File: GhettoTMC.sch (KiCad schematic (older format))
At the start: 48 parts

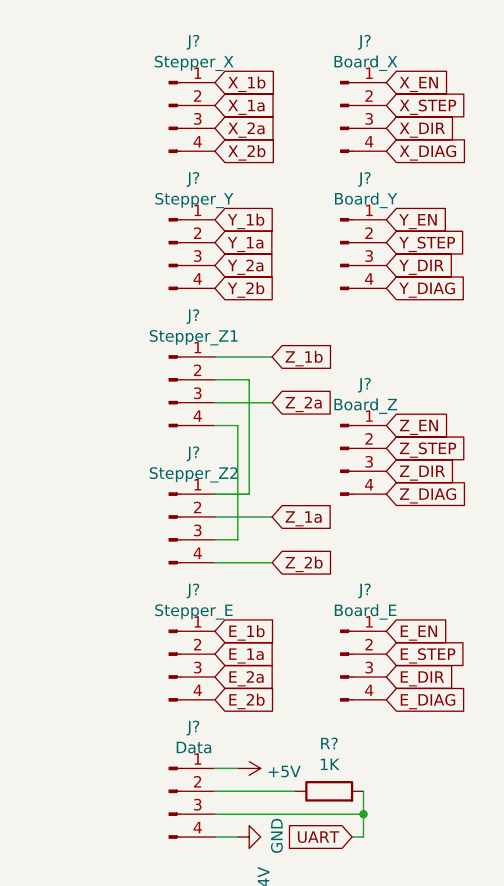
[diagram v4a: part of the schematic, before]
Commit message: Switch to 5p Board connectors
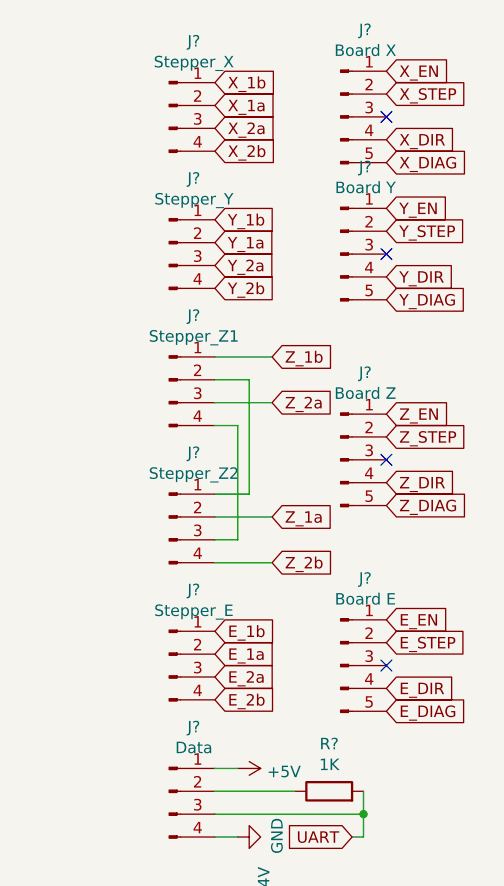
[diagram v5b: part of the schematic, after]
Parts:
- removed J?: Board_Y, GhettoTMC:MOLEX_70553-0038, symbol Connector:Conn_01x04_Male
- removed J?: Board_X, GhettoTMC:MOLEX_70553-0038, symbol Connector:Conn_01x04_Male
- removed J?: Board_Z, GhettoTMC:MOLEX_70553-0038, symbol Connector:Conn_01x04_Male
- removed J?: Board_E, GhettoTMC:MOLEX_70553-0038, symbol Connector:Conn_01x04_Male
- added J?: Board X, GhettoTMC:MOLEX_70553-0039, symbol Connector:Conn_01x05_Male
- added J?: Board Y, GhettoTMC:MOLEX_70553-0039, symbol Connector:Conn_01x05_Male
- added J?: Board Z, GhettoTMC:MOLEX_70553-0039, symbol Connector:Conn_01x05_Male
- added J?: Board E, GhettoTMC:MOLEX_70553-0039, symbol Connector:Conn_01x05_Male
- J?: footprint (none) -> Connectors_Phoenix:PhoenixContact_MC-G_02x5.08mm_Angled
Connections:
- net E_DIAG: now also J?.5 (Pin_5)
- net E_DIR: now also J?.4 (Pin_4)
- net E_EN: now also J?.1 (Pin_1)
- net E_STEP: now also J?.2 (Pin_2)
- net X_DIAG: now also J?.5 (Pin_5)
- net X_DIR: now also J?.4 (Pin_4)
- net X_EN: now also J?.1 (Pin_1)
- net X_STEP: now also J?.2 (Pin_2)
- net Y_DIAG: now also J?.5 (Pin_5)
- net Y_DIR: now also J?.4 (Pin_4)
- net Y_EN: now also J?.1 (Pin_1)
- net Y_STEP: now also J?.2 (Pin_2)
- net Z_DIAG: now also J?.5 (Pin_5)
- net Z_DIR: now also J?.4 (Pin_4)
- net Z_EN: now also J?.1 (Pin_1)
- net Z_STEP: now also J?.2 (Pin_2)
- no-connect marks 4 -> 8
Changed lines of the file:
@@
 	10000 4350 10000 4250
 Connection ~ 10000 4250
-$Comp
-L Connector:Conn_01x04_Male J?
-U 1 1 5EAC38CC
-P 9900 1750
-F 0 "J?" H 10008 2031 50  0000 C CNN
-F 1 "Board_Y" H 10008 1940 50  0000 C CNN
-F 2 "GhettoTMC:MOLEX_70553-0038" H 9900 1750 50  0001 C CNN
-F 3 "~" H 9900 1750 50  0001 C CNN
-	1    9900 1750
-	1    0    0    -1
-$EndComp
-$Comp
-L Connector:Conn_01x04_Male J?
-U 1 1 5EAC4D8C
-P 9900 1150
-F 0 "J?" H 10008 1431 50  0000 C CNN
-F 1 "Board_X" H 10008 1340 50  0000 C CNN
-F 2 "GhettoTMC:MOLEX_70553-0038" H 9900 1150 50  0001 C CNN
-F 3 "~" H 9900 1150 50  0001 C CNN
-	1    9900 1150
-	1    0    0    -1
-$EndComp
-$Comp
-L Connector:Conn_01x04_Male J?
-U 1 1 5EAC51EC
-P 9900 2650
-F 0 "J?" H 10008 2931 50  0000 C CNN
-F 1 "Board_Z" H 10008 2840 50  0000 C CNN
-F 2 "GhettoTMC:MOLEX_70553-0038" H 9900 2650 50  0001 C CNN
-F 3 "~" H 9900 2650 50  0001 C CNN
-	1    9900 2650
-	1    0    0    -1
-$EndComp
-$Comp
-L Connector:Conn_01x04_Male J?
-U 1 1 5EAC5E5C
-P 9900 3550
-F 0 "J?" H 10008 3831 50  0000 C CNN
-F 1 "Board_E" H 10008 3740 50  0000 C CNN
-F 2 "GhettoTMC:MOLEX_70553-0038" H 9900 3550 50  0001 C CNN
-F 3 "~" H 9900 3550 50  0001 C CNN
-	1    9900 3550
-	1    0    0    -1
-$EndComp
-Text GLabel 10100 1950 2    50   Input ~ 0
+Text GLabel 10100 2000 2    50   Input ~ 0
 Y_DIAG
-Text GLabel 10100 1850 2    50   Input ~ 0
+Text GLabel 10100 1900 2    50   Input ~ 0
 Y_DIR
-Text GLabel 10100 1650 2    50   Input ~ 0
+Text GLabel 10100 1600 2    50   Input ~ 0
 Y_EN
-Text GLabel 10100 1750 2    50   Input ~ 0
+Text GLabel 10100 1700 2    50   Input ~ 0
 Y_STEP
-Text GLabel 10100 1350 2    50   Input ~ 0
+Text GLabel 10100 1400 2    50   Input ~ 0
 X_DIAG
-Text GLabel 10100 1250 2    50   Input ~ 0
+Text GLabel 10100 1300 2    50   Input ~ 0
 X_DIR
-Text GLabel 10100 1050 2    50   Input ~ 0
+Text GLabel 10100 1000 2    50   Input ~ 0
 X_EN
-Text GLabel 10100 1150 2    50   Input ~ 0
+Text GLabel 10100 1100 2    50   Input ~ 0
 X_STEP
-Text GLabel 10100 2850 2    50   Input ~ 0
+Text GLabel 10100 2900 2    50   Input ~ 0
 Z_DIAG
-Text GLabel 10100 2750 2    50   Input ~ 0
+Text GLabel 10100 2800 2    50   Input ~ 0
 Z_DIR
-Text GLabel 10100 2550 2    50   Input ~ 0
+Text GLabel 10100 2500 2    50   Input ~ 0
 Z_EN
-Text GLabel 10100 2650 2    50   Input ~ 0
+Text GLabel 10100 2600 2    50   Input ~ 0
 Z_STEP
-Text GLabel 10100 3750 2    50   Input ~ 0
+Text GLabel 10100 3800 2    50   Input ~ 0
 E_DIAG
-Text GLabel 10100 3650 2    50   Input ~ 0
+Text GLabel 10100 3700 2    50   Input ~ 0
 E_DIR
-Text GLabel 10100 3450 2    50   Input ~ 0
+Text GLabel 10100 3400 2    50   Input ~ 0
 E_EN
-Text GLabel 10100 3550 2    50   Input ~ 0
+Text GLabel 10100 3500 2    50   Input ~ 0
 E_STEP
 $Comp
@@
 F 0 "J?" H 9258 4981 50  0000 C CNN
 F 1 "POWER IN" H 9258 4890 50  0000 C CNN
-F 2 "" H 9150 4800 50  0001 C CNN
+F 2 "Connectors_Phoenix:PhoenixContact_MC-G_02x5.08mm_Angled" H 9150 4800 50  0001 C CNN
 F 3 "~" H 9150 4800 50  0001 C CNN
 	1    9150 4800
@@
 	1    0    0    -1
 $EndComp
+NoConn ~ 10100 1200
+$Comp
+L Connector:Conn_01x05_Male J?
+U 1 1 5EB3A24B
+P 9900 1800
+F 0 "J?" H 10008 2181 50  0000 C CNN
+F 1 "Board Y" H 10008 2090 50  0000 C CNN
+F 2 "GhettoTMC:MOLEX_70553-0039" H 9900 1800 50  0001 C CNN
+F 3 "~" H 9900 1800 50  0001 C CNN
+	1    9900 1800
+	1    0    0    -1
+$EndComp
+NoConn ~ 10100 1800
+$Comp
+L Connector:Conn_01x05_Male J?
+U 1 1 5EB41CC3
+P 9900 2700
+F 0 "J?" H 10008 3081 50  0000 C CNN
+F 1 "Board Z" H 10008 2990 50  0000 C CNN
+F 2 "GhettoTMC:MOLEX_70553-0039" H 9900 2700 50  0001 C CNN
+F 3 "~" H 9900 2700 50  0001 C CNN
+	1    9900 2700
+	1    0    0    -1
+$EndComp
+NoConn ~ 10100 2700
+$Comp
+L Connector:Conn_01x05_Male J?
+U 1 1 5EB49933
+P 9900 3600
+F 0 "J?" H 10008 3981 50  0000 C CNN
+F 1 "Board E" H 10008 3890 50  0000 C CNN
+F 2 "GhettoTMC:MOLEX_70553-0039" H 9900 3600 50  0001 C CNN
+F 3 "~" H 9900 3600 50  0001 C CNN
+	1    9900 3600
+	1    0    0    -1
+$EndComp
+NoConn ~ 10100 3600
+$Comp
+L Connector:Conn_01x05_Male J?
+U 1 1 5EB1718C
+P 9900 1200
+F 0 "J?" H 10008 1581 50  0000 C CNN
+F 1 "Board X" H 10008 1490 50  0000 C CNN
+F 2 "GhettoTMC:MOLEX_70553-0039" H 9900 1200 50  0001 C CNN
+F 3 "~" H 9900 1200 50  0001 C CNN
+	1    9900 1200
+	1    0    0    -1
+$EndComp

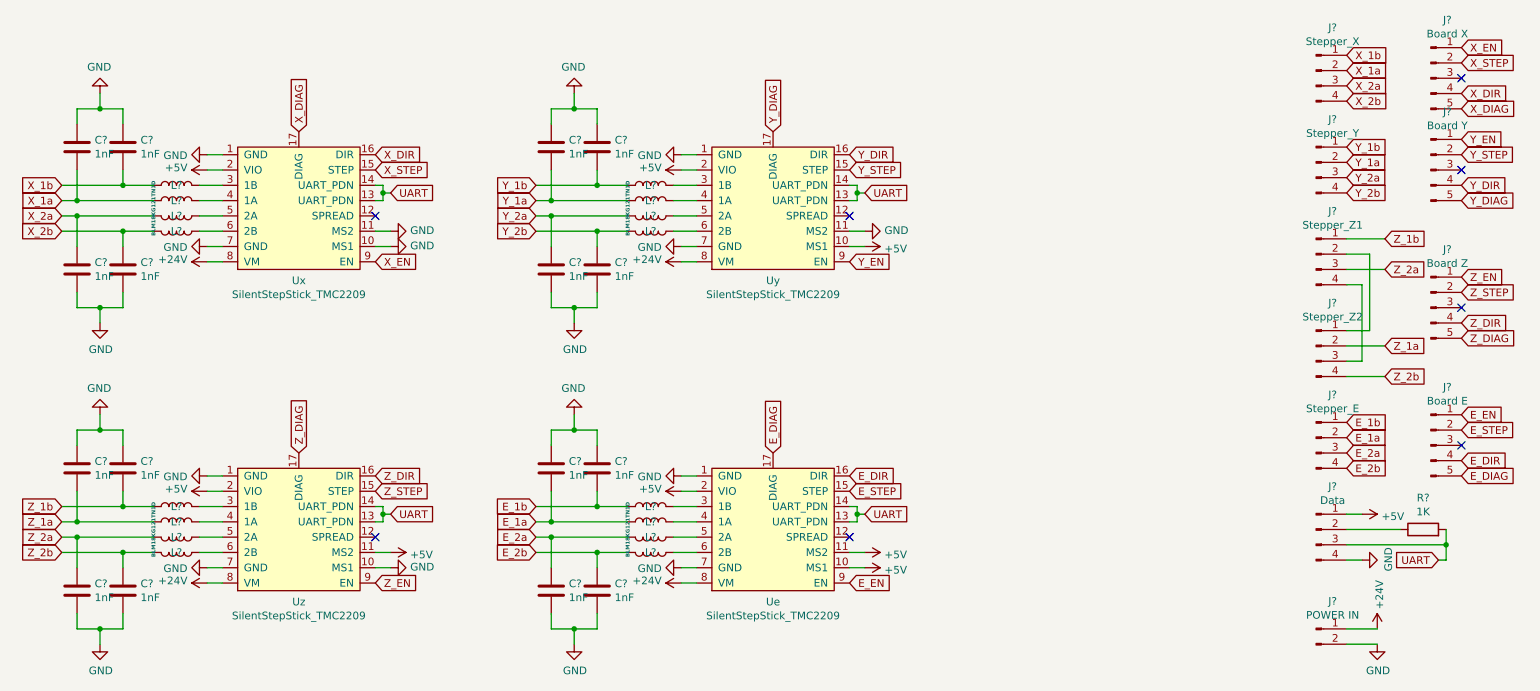
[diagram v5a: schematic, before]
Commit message: Assign footprints
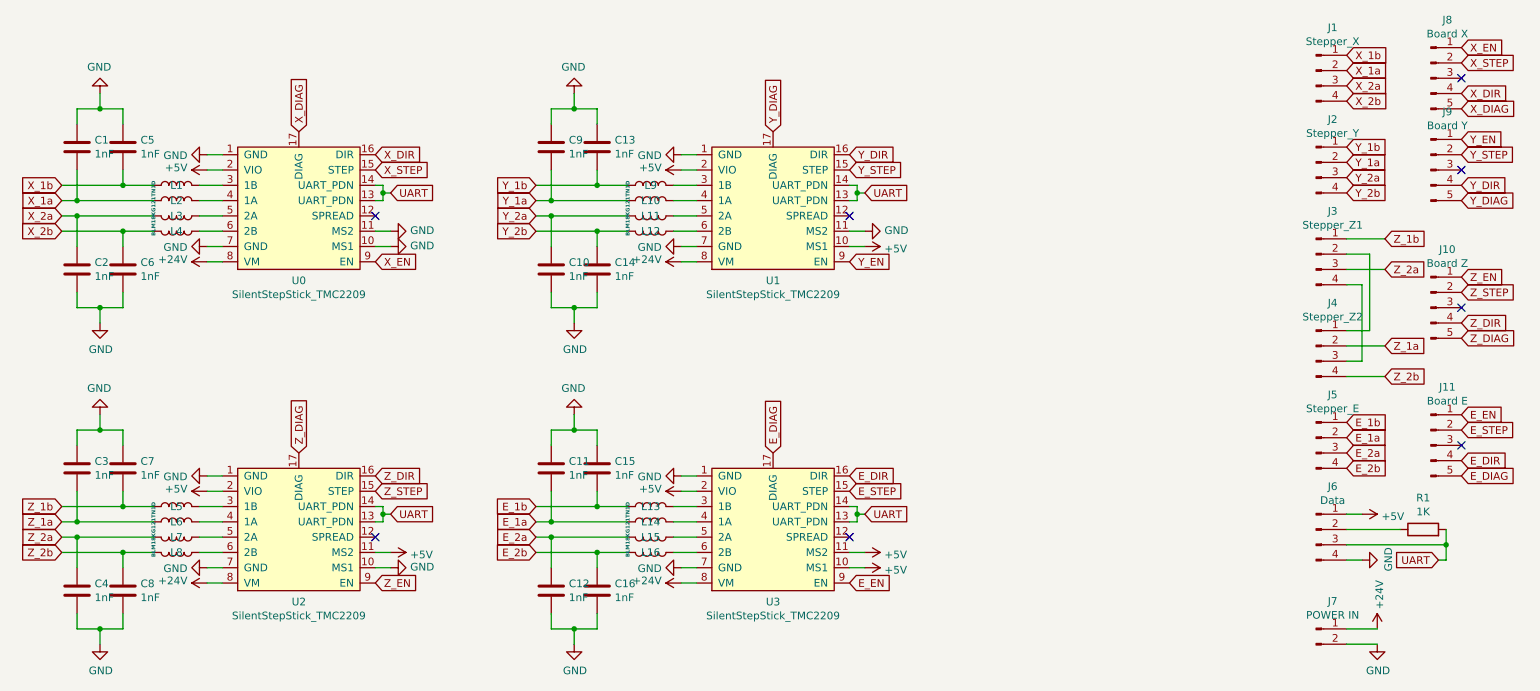
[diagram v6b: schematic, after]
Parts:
- C1, C10, C11, C12, C13, C14, C15, C16, C2, C3, C4, C5, C6, C7, C8, C9: renamed from C?; footprint (none) -> Capacitor_THT:C_Disc_D6.0mm_W2.5mm_P5.00mm
- L1, L10, L11, L12, L13, L14, L15, L16, L2, L3, L4, L5, L6, L7, L8, L9: renamed from L?; footprint (none) -> Inductor_SMD:L_0603_1608Metric_Pad1.05x0.95mm_HandSolder
- R1: renamed from R?; footprint (none) -> Resistor_THT:R_Axial_DIN0207_L6.3mm_D2.5mm_P10.16mm_Horizontal
- U0: renamed from Ux; footprint (none) -> GhettoTMC:SilentStepStick_TMC2209_Breakout
- U1: renamed from Uy; footprint (none) -> GhettoTMC:SilentStepStick_TMC2209_Breakout
- U2: renamed from Uz; footprint (none) -> GhettoTMC:SilentStepStick_TMC2209_Breakout
- U3: renamed from Ue; footprint (none) -> GhettoTMC:SilentStepStick_TMC2209_Breakout
- gave numbers to parts that had none: 11

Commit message: Update power connector footprint in schematic
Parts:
- J7: footprint Connectors_Phoenix:PhoenixContact_MC-G_02x5.08mm_Angled -> GhettoTMC:PhoenixContact_MC-G_02x5.08mm_Angled
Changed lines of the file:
@@
 F 0 "J7" H 9258 4981 50  0000 C CNN
 F 1 "POWER IN" H 9258 4890 50  0000 C CNN
-F 2 "Connectors_Phoenix:PhoenixContact_MC-G_02x5.08mm_Angled" H 9150 4800 50  0001 C CNN
+F 2 "GhettoTMC:PhoenixContact_MC-G_02x5.08mm_Angled" H 9150 4800 50  0001 C CNN
 F 3 "~" H 9150 4800 50  0001 C CNN
 	1    9150 4800
